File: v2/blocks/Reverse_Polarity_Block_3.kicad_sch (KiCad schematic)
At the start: 5 parts, among them Q7 AP25P06K

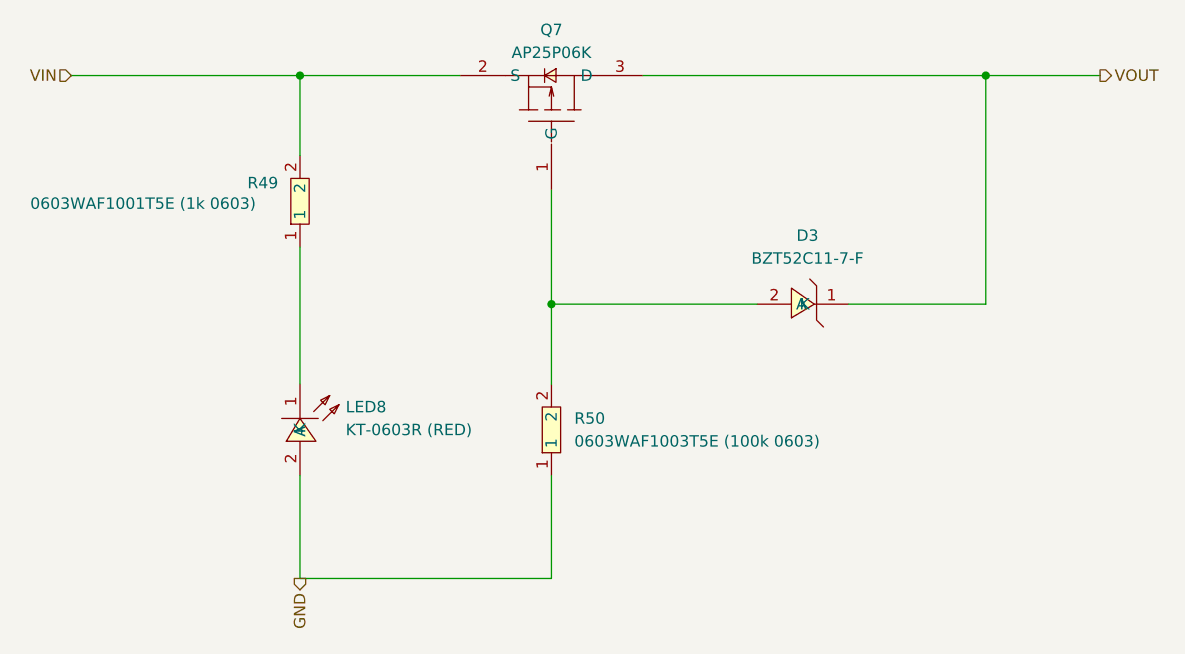
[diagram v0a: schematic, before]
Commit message: preliminary layout
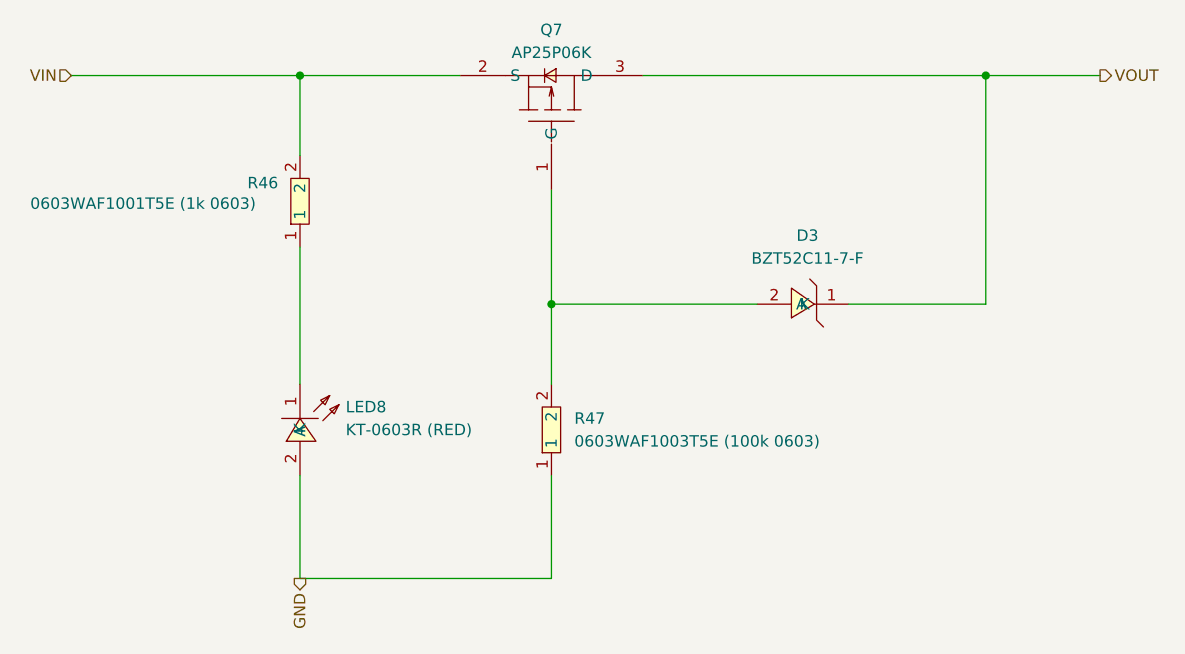
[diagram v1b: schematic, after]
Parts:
- renumbered R49 to R46, R50 to R47
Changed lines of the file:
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@@
 		(dnp no)
 		(fields_autoplaced yes)
-		(property "Reference" "R50"
+		(property "Reference" "R47"
 			(at 132.08 101.5999 90)
 			(effects
@@
 			(project "EPSv2"
 				(path "/61d36b12-c329-4dd2-b08b-b63678fc7b25/2039548c-fd43-41af-9eb1-e8200f7b5bef"
-					(reference "R50")
+					(reference "R47")
 					(unit 1)
 				)
@@
 		(on_board yes)
 		(dnp no)
-		(property "Reference" "R49"
+		(property "Reference" "R46"
 			(at 95.758 75.438 90)
 			(effects
@@
 			(project "EPSv2"
 				(path "/61d36b12-c329-4dd2-b08b-b63678fc7b25/2039548c-fd43-41af-9eb1-e8200f7b5bef"
-					(reference "R49")
+					(reference "R46")
 					(unit 1)
 				)

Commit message: routing done
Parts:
- renumbered D3 to D7, R46 to R54, R47 to R55
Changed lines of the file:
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@@
 		(dnp no)
 		(fields_autoplaced yes)
-		(property "Reference" "R47"
+		(property "Reference" "R55"
 			(at 132.08 101.5999 90)
 			(effects
@@
 			(project "EPSv2"
 				(path "/61d36b12-c329-4dd2-b08b-b63678fc7b25/2039548c-fd43-41af-9eb1-e8200f7b5bef"
-					(reference "R47")
+					(reference "R55")
 					(unit 1)
 				)
@@
 		(on_board yes)
 		(dnp no)
-		(property "Reference" "R46"
+		(property "Reference" "R54"
 			(at 95.758 75.438 90)
 			(effects
@@
 			(project "EPSv2"
 				(path "/61d36b12-c329-4dd2-b08b-b63678fc7b25/2039548c-fd43-41af-9eb1-e8200f7b5bef"
-					(reference "R46")
+					(reference "R54")
 					(unit 1)
 				)
@@
 		(dnp no)
 		(fields_autoplaced yes)
-		(property "Reference" "D3"
+		(property "Reference" "D7"
 			(at 157.99 81.28 0)
 			(effects
@@
 			(project "EPSv2"
 				(path "/61d36b12-c329-4dd2-b08b-b63678fc7b25/2039548c-fd43-41af-9eb1-e8200f7b5bef"
-					(reference "D3")
-					(unit 1)
-				)
+					(reference "D7")
+					(unit 1)
+				)

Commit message: CAN txrx
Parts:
- renumbered D7 to D9, R54 to R61, R55 to R62
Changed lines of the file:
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@@
 		(shape output)
 		(at 101.6 119.38 270)
-		(fields_autoplaced yes)
 		(effects
 			(font
@@
 		(shape input)
 		(at 76.2 63.5 180)
-		(fields_autoplaced yes)
 		(effects
 			(font
@@
 		(shape output)
 		(at 190.5 63.5 0)
-		(fields_autoplaced yes)
 		(effects
 			(font
@@
 		(dnp no)
 		(fields_autoplaced yes)
-		(property "Reference" "R55"
+		(property "Reference" "R62"
 			(at 132.08 101.5999 90)
 			(effects
@@
 			(project "EPSv2"
 				(path "/61d36b12-c329-4dd2-b08b-b63678fc7b25/2039548c-fd43-41af-9eb1-e8200f7b5bef"
-					(reference "R55")
+					(reference "R62")
 					(unit 1)
 				)
@@
 		(on_board yes)
 		(dnp no)
-		(property "Reference" "R54"
+		(property "Reference" "R61"
 			(at 95.758 75.438 90)
 			(effects
@@
 			(project "EPSv2"
 				(path "/61d36b12-c329-4dd2-b08b-b63678fc7b25/2039548c-fd43-41af-9eb1-e8200f7b5bef"
-					(reference "R54")
+					(reference "R61")
 					(unit 1)
 				)
@@
 		(dnp no)
 		(fields_autoplaced yes)
-		(property "Reference" "D7"
+		(property "Reference" "D9"
 			(at 157.99 81.28 0)
 			(effects
@@
 			(project "EPSv2"
 				(path "/61d36b12-c329-4dd2-b08b-b63678fc7b25/2039548c-fd43-41af-9eb1-e8200f7b5bef"
-					(reference "D7")
-					(unit 1)
-				)
+					(reference "D9")
+					(unit 1)
+				)

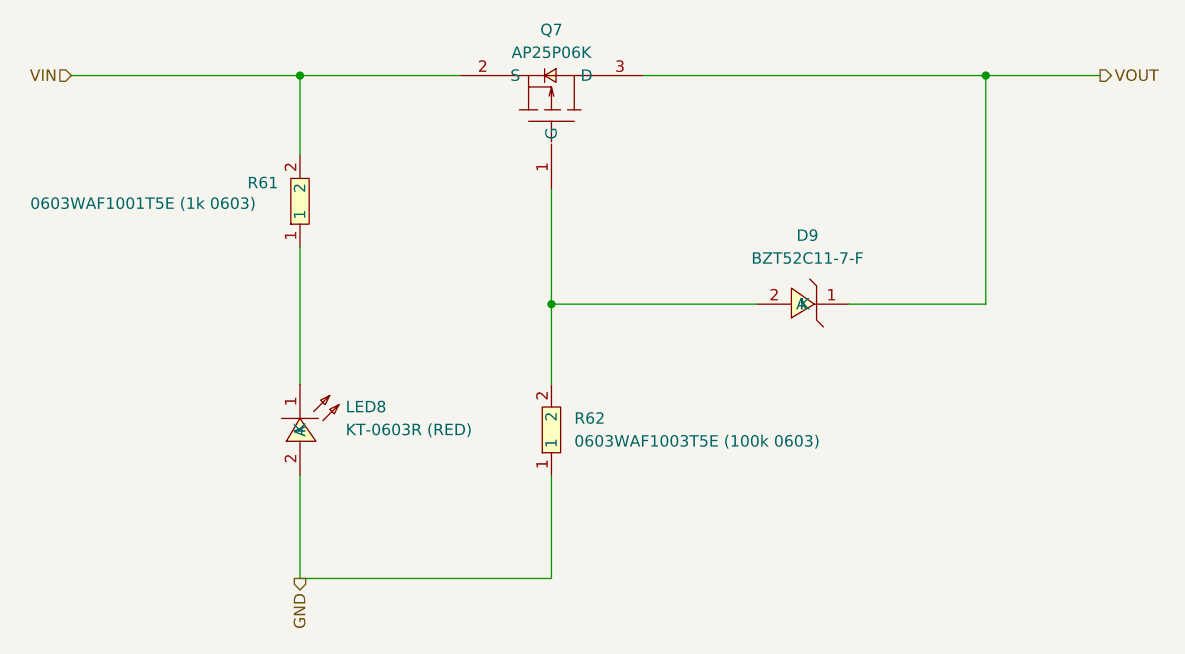
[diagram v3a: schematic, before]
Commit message: can transceiver and battery reverse polarity bypass
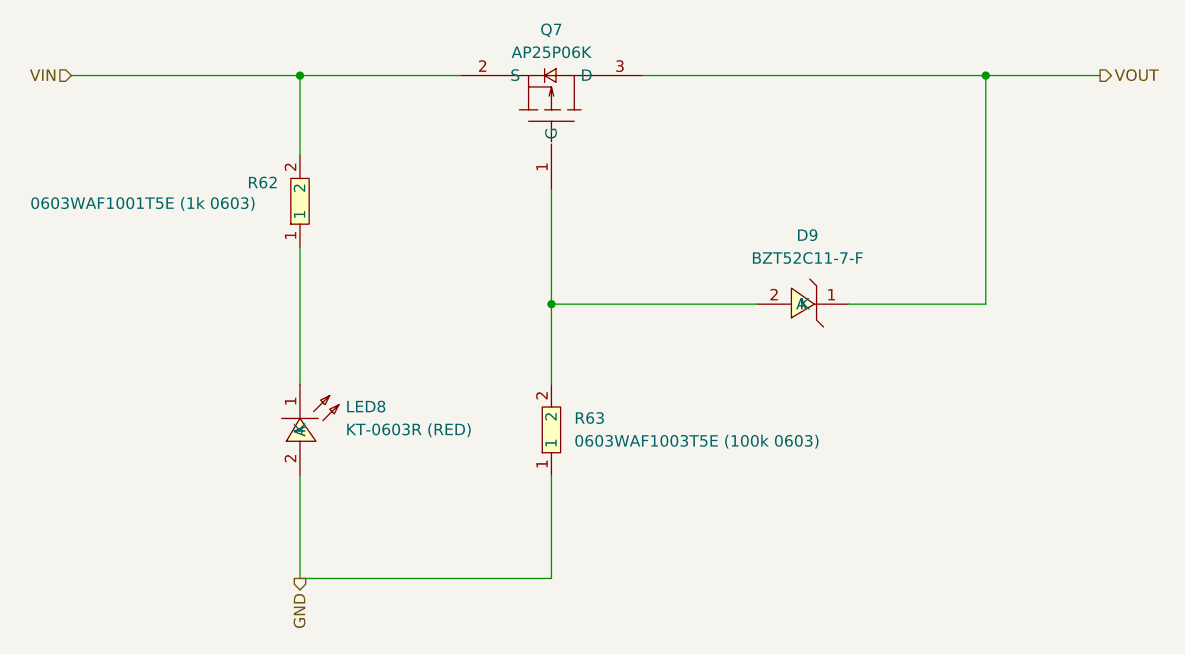
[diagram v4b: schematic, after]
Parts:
- renumbered R61 to R62, R62 to R63
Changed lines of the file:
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@@
 		(shape output)
 		(at 101.6 119.38 270)
+		(fields_autoplaced yes)
 		(effects
 			(font
@@
 		(shape input)
 		(at 76.2 63.5 180)
+		(fields_autoplaced yes)
 		(effects
 			(font
@@
 		(shape output)
 		(at 190.5 63.5 0)
+		(fields_autoplaced yes)
 		(effects
 			(font
@@
 		(dnp no)
 		(fields_autoplaced yes)
-		(property "Reference" "R62"
+		(property "Reference" "R63"
 			(at 132.08 101.5999 90)
 			(effects
@@
 			(project "EPSv2"
 				(path "/61d36b12-c329-4dd2-b08b-b63678fc7b25/2039548c-fd43-41af-9eb1-e8200f7b5bef"
-					(reference "R62")
+					(reference "R63")
 					(unit 1)
 				)
@@
 		(on_board yes)
 		(dnp no)
-		(property "Reference" "R61"
+		(property "Reference" "R62"
 			(at 95.758 75.438 90)
 			(effects
@@
 			(project "EPSv2"
 				(path "/61d36b12-c329-4dd2-b08b-b63678fc7b25/2039548c-fd43-41af-9eb1-e8200f7b5bef"
-					(reference "R61")
+					(reference "R62")
 					(unit 1)
 				)

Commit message: bigger current ratings for 5V and 9V
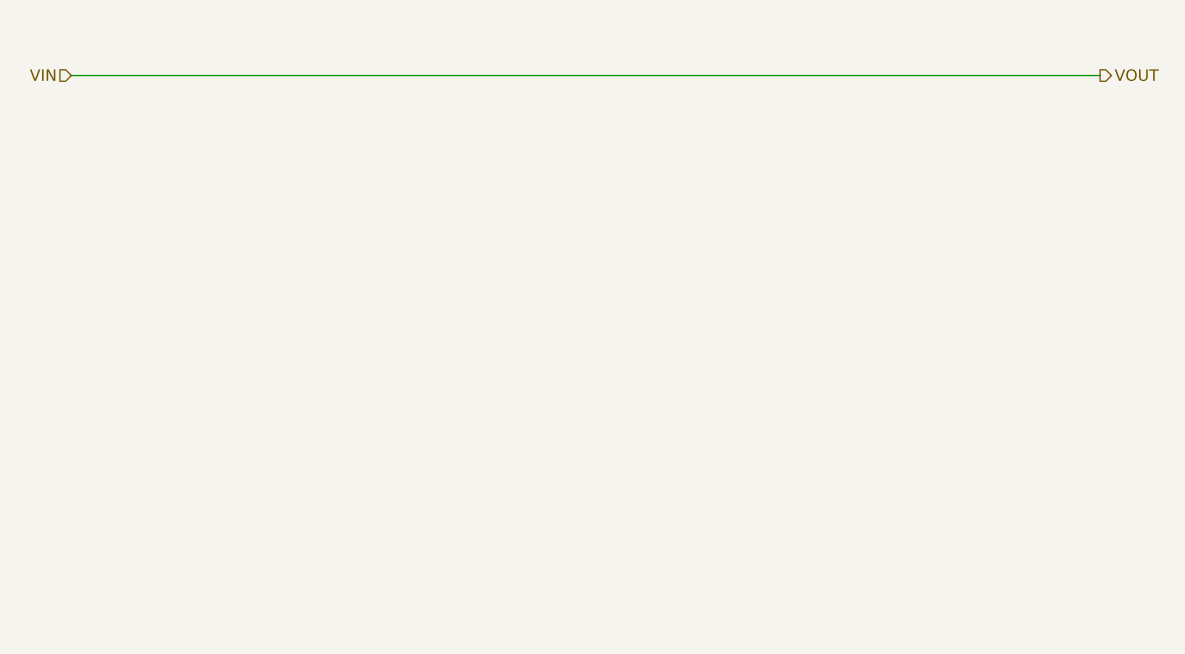
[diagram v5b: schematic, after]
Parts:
- removed D9: BZT52C11-7-F, Rocketry_Easyeda:SOD-123_L2.8-W1.8-LS3.7-RD, symbol Rocketry_Easyeda:BZT52C11-7-F
- removed LED8: KT-0603R (RED), Rocketry_Easyeda:LED0603-RD, symbol Rocketry_Easyeda:KT-0603R
- removed Q7: AP25P06K, Rocketry_Easyeda:TO-252-2_L6.6-W6.1-P4.57-LS10.1-BL, symbol Rocketry_Easyeda:AP25P06K
- removed R62: 0603WAF1001T5E (1k 0603), Rocketry_Easyeda:R0603, symbol Rocketry_Easyeda:0603WAF1001T5E (1k 0603)
- removed R63: 0603WAF1003T5E (100k 0603), Rocketry_Easyeda:R0603, symbol Rocketry_Easyeda:0603WAF1003T5E (100k 0603)
